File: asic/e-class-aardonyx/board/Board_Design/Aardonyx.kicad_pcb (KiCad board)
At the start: 4 copper layers, 298 parts, among them J1 USB_B_6PIN, J10 Conn_1x6_F, J11 Conn_1x6_F, J12 Conn_1x3_M, J13 Conn_1x8_F, J14 Conn_1x6_F, J15 Conn_1x10, J16 Conn_1x8_F, J17 USB_OTG, J18 Conn_1x3_M, J19 Conn_1x3_M, J2 Conn_1x8, J3 Conn_1x3_M, J4 Conn_1x4, J5 PJ-202H PWRJACK, J6 Conn_1x3_M, J7 Conn_1x4, J8 Conn_1x3_M, J9 Conn_1x8, Q1 FDN339AN, SW1 SW_SPST, SW2 FSM2JSMAATR, SW3 SW_DIP_x03, U1 FT2232H, U10 TPS7A7002DDAR, U11 ADM1085, U12 ADM1085, U13 TPS7A7002DDAR, U14 74AUP1G09GW, U15 SKT32E, U16 93LC56BT-I_OT, U2 IS42S32160F-TSOP2, U3 CDCE913PW, U4 TPS54627DDAR, U5 CAT24M01WI-GT3, U6 IS25LP256x-xM, U7 ADC108S102CIMTX, U8 LSF0108PWR, U9 LSF0108PWR, Y1 12MHz, Y2 27MHz

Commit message: Placement changes
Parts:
- moved R128 129.7 mm to (202.0, 117.0)
- moved R129 129.7 mm to (205.0, 116.9)
- moved R131 129.7 mm to (202.2, 132.6)
- moved R132 129.7 mm to (204.2, 132.6)
- moved R130 129.7 mm to (208.3, 117.0)
- moved SW3 129.7 mm to (207.5, 121.1)
- moved J11 122.3 mm to (182.1, 160.3), turned to 90 degrees
- moved J12 108.9 mm to (152.7, 150.6)
- moved U7 106.0 mm to (120.7, 146.1), turned to 90 degrees
- moved C49 103.3 mm to (117.6, 146.1)
- moved C50 103.3 mm to (130.3, 146.6)
- moved R35 103.3 mm to (117.6, 142.6)
- moved J19 80.7 mm to (147.3, 150.6), turned to 0 degrees
- moved J8 59.6 mm to (207.0, 99.6)
- moved J9 56.5 mm to (196.6, 107.7)
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
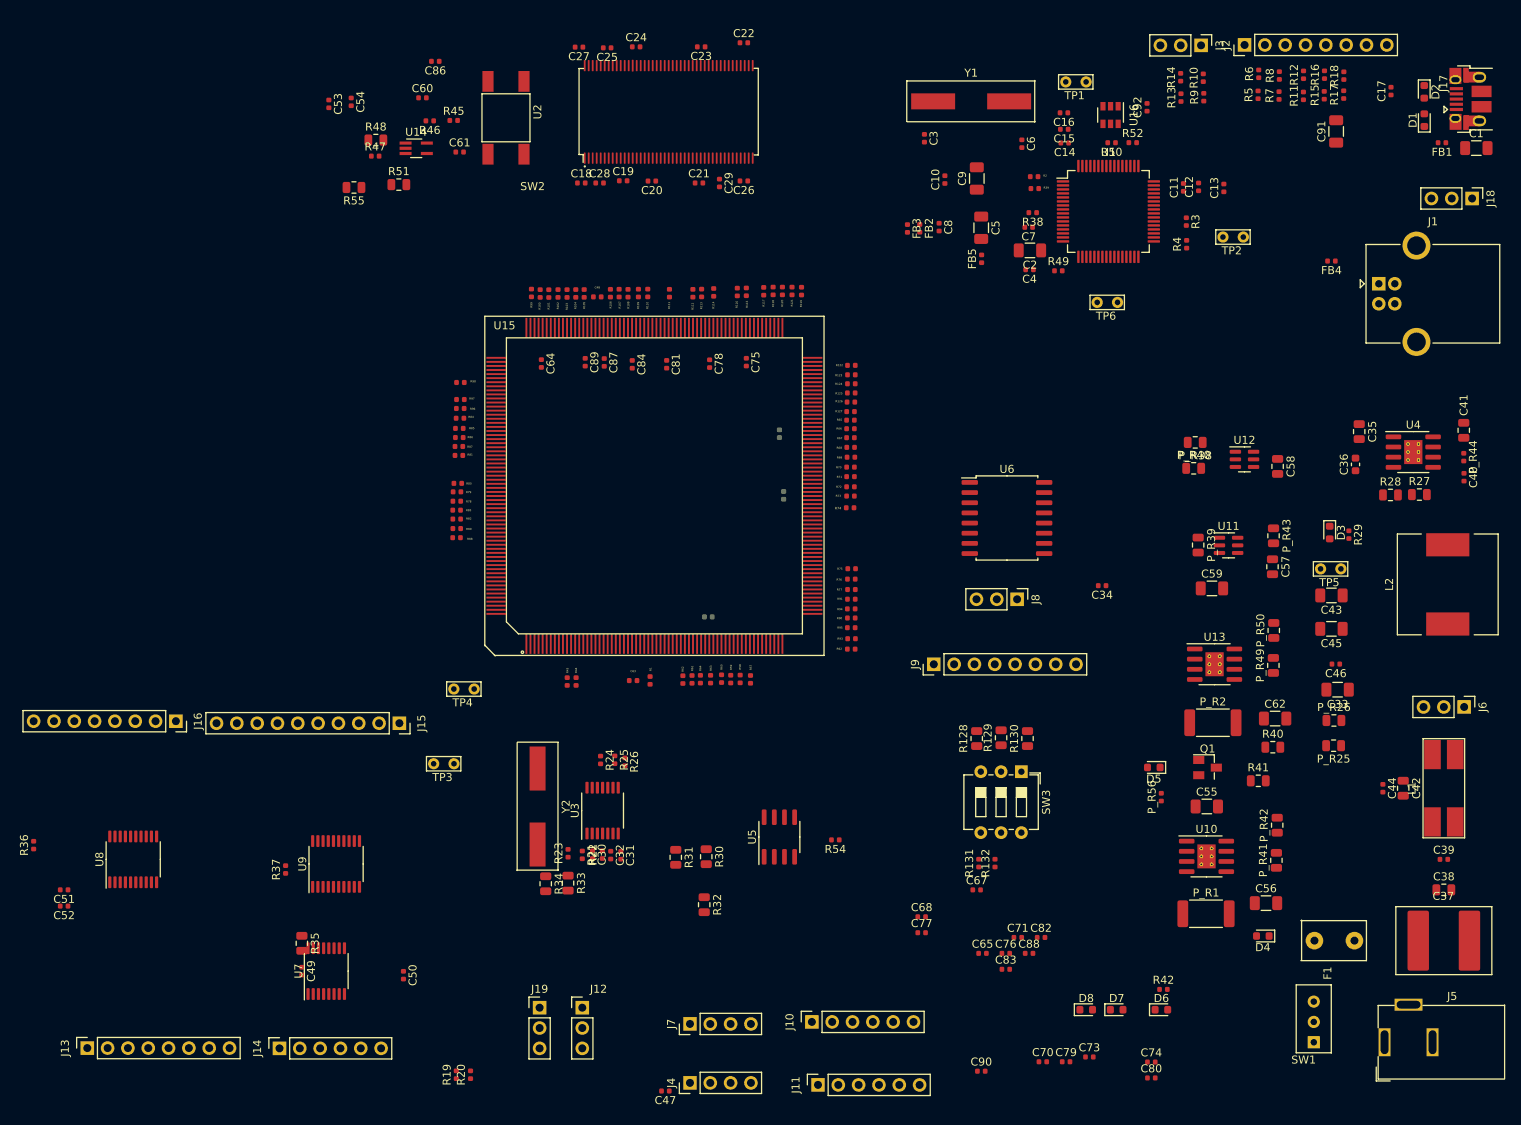
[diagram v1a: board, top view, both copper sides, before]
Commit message: updated compo placement
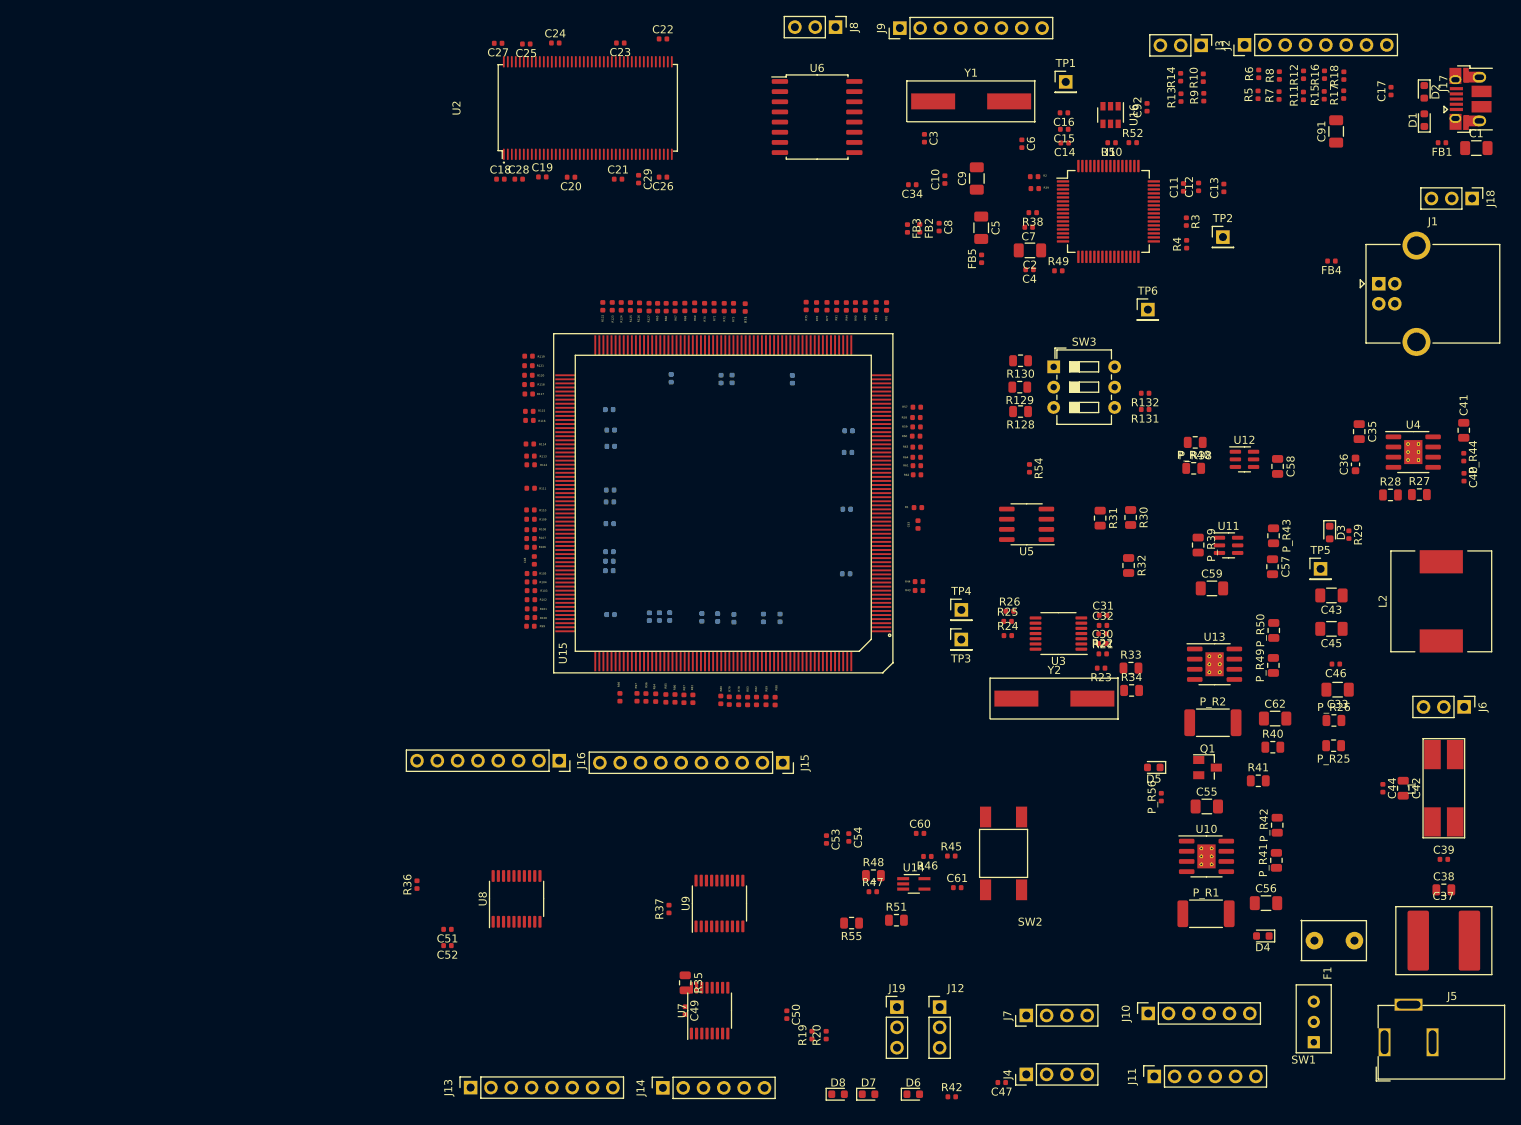
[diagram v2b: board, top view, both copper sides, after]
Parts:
- C64, C65, C67, C68, C70, C71, C73, C74, C75, C76, C77, C78, C79, C80, C81, C82, C83, C84, C86, C87, C88, C89, C90: moved to B.Cu
- TP1, TP2, TP3, TP4, TP5, TP6: footprint TestPoint:TestPoint_Bridge_Pitch2.54mm_Drill0.7mm -> Connector_PinHeader_2.54mm:PinHeader_1x01_P2.54mm_Vertical
- moved C60 111.0 mm to (194.9, 128.8)
- moved C61 111.0 mm to (199.5, 135.6)
- moved C53 111.0 mm to (183.2, 129.6)
- moved R46 111.0 mm to (195.8, 131.7)
- moved R48 111.0 mm to (189.0, 134.1)
- moved R51 111.0 mm to (191.9, 139.7)
- moved SW2 111.0 mm to (205.3, 131.3)
- moved C54 111.0 mm to (186.0, 129.3)
- moved R45 111.0 mm to (198.8, 131.7)
- moved R47 111.0 mm to (189.0, 136.1)
- moved R55 111.0 mm to (186.3, 140.0)
- moved U14 111.0 mm to (194.1, 135.1)
- moved C80 105.5 mm to (156.2, 78.4)
- moved C74 96.4 mm to (178.9, 72.1), turned to 270 degrees
- moved J9 79.6 mm to (192.3, 28.2)
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
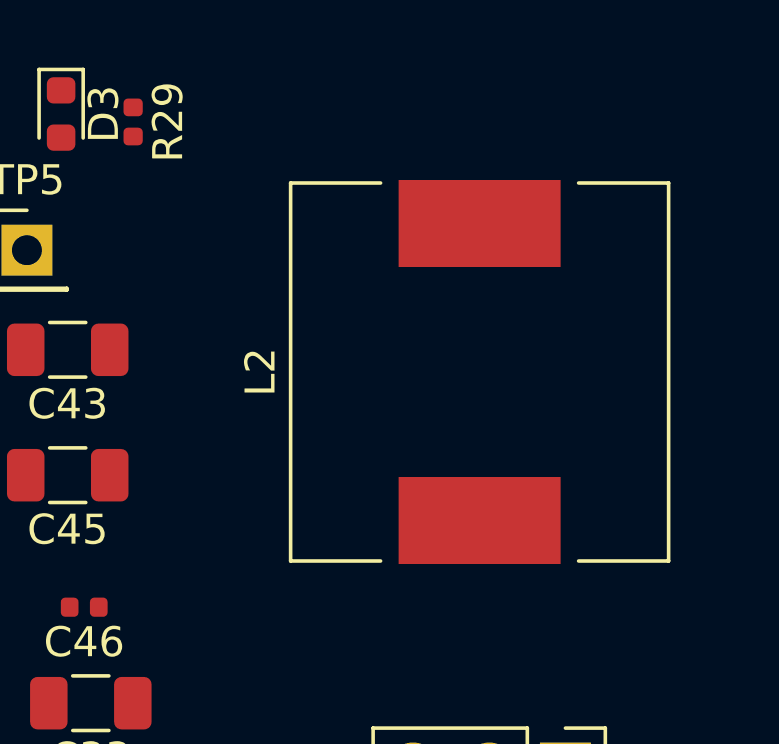
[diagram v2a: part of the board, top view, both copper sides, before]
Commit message: update footprint & bom
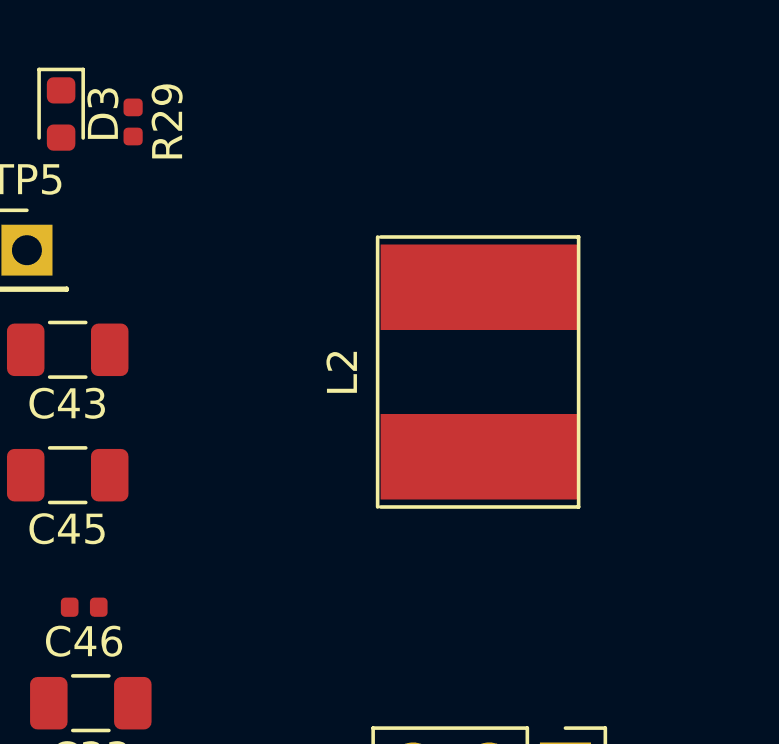
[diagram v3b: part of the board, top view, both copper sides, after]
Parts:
- L2: footprint Inductor_SMD:L_Wuerth_WE-PD-Typ-LS -> Aardonyx:Bourns_srn8040ta_L8.5_W6.6
- U7: value ADC108S102CIMTX -> ADC128S102CIMTX/NOPB
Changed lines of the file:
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@@
     (add_net ~)
   )
+  (module Aardonyx:Bourns_srn8040ta_L8.5_W6.6 (layer F.Cu)
+    (at 260.03 99.83 90)
+    (descr "Shielded Coupled Inductor, Wuerth Elektronik, WE-DD, SMD, Typ L, Typ XL, Typ XXL, https://katalog.we-online.com/pbs/datasheet/744874001.pdf")
+    (tags "Choke Coupled Double Inductor SMD Wuerth WE-DD TypL TypXL TypXXL ")
+    (attr smd)
+    (fp_text reference L2 (at -0.01016 -4.55168 90) (layer F.SilkS)
+      (effects (font (size 1 1) (thickness 0.15)))
+    )
+    (fp_text value 3.3UH (at -0.04572 4.54152 90) (layer F.Fab)
+      (effects (font (size 1 1) (thickness 0.15)))
+    )
+    (fp_line (start -4.3 -3.4) (end 4.3 -3.4) (layer F.Fab) (width 0.1))
+    (fp_line (start -4.3 3.3) (end -4.3 -3.3) (layer F.Fab) (width 0.1))
+    (fp_line (start 4.3 3.3) (end -4.3 3.3) (layer F.Fab) (width 0.1))
+    (fp_line (start 4.3 -3.3) (end 4.3 3.3) (layer F.Fab) (width 0.1))
+    (fp_line (start -4.5 3.3) (end -4.5 -3.3) (layer F.SilkS) (width 0.12))
+    (fp_line (start 4.5 3.3) (end -4.5 3.3) (layer F.SilkS) (width 0.12))
+    (fp_line (start 4.5 -3.3) (end 4.5 3.3) (layer F.SilkS) (width 0.12))
+    (fp_line (start -4.5 -3.4) (end 4.5 -3.4) (layer F.SilkS) (width 0.12))
+    (pad 2 smd rect (at 2.825 0 90) (size 2.85 6.6) (layers F.Cu F.Paste F.Mask)
+      (net 425 ~))
+    (pad 1 smd rect (at -2.825 0 90) (size 2.85 6.6) (layers F.Cu F.Paste F.Mask)
+      (net 11 "Net-(C40-Pad2)"))
+    (model ${KISYS3DMOD}/Inductor_SMD.3dshapes/L_Wuerth_WE-DD-Typ-L-Typ-XL-Typ-XXL.wrl
+      (at (xyz 0 0 0))
+      (scale (xyz 1 1 1))
+      (rotate (xyz 0 0 0))
+    )
+  )
   (module Connector_PinHeader_2.54mm:PinHeader_1x01_P2.54mm_Vertical (layer F.Cu)
     (at 223.35 63.36)
@@
     )
   )
-  (module Inductor_SMD:L_Wuerth_WE-PD-Typ-LS (layer F.Cu)
-    (at 260.03 99.83 90)
-    (descr "Shielded Power Inductor, Wuerth Elektronik, WE-PD, SMD, Typ LS, https://katalog.we-online.com/pbs/datasheet/7447715906.pdf")
-    (tags "Choke Shielded Power Inductor WE-PD TypLS Wuerth")
-    (attr smd)
-    (fp_text reference L2 (at 0 -7.3 90) (layer F.SilkS)
-      (effects (font (size 1 1) (thickness 0.15)))
-    )
-    (fp_text value 3.3UH (at 0 7.4 90) (layer F.Fab)
-      (effects (font (size 1 1) (thickness 0.15)))
-    )
-    (fp_line (start -6.2 -6.2) (end -6.2 6.2) (layer F.Fab) (width 0.1))
-    (fp_line (start 6.2 6.2) (end 6.2 -6.2) (layer F.Fab) (width 0.1))
-    (fp_line (start -6.3 -3.3) (end -6.3 -6.3) (layer F.SilkS) (width 0.12))
-    (fp_line (start -6.3 -6.3) (end 6.3 -6.3) (layer F.SilkS) (width 0.12))
-    (fp_line (start 6.3 -6.3) (end 6.3 -3.3) (layer F.SilkS) (width 0.12))
-    (fp_line (start 6.3 3.3) (end 6.3 6.3) (layer F.SilkS) (width 0.12))
-    (fp_line (start 6.3 6.3) (end -6.3 6.3) (layer F.SilkS) (width 0.12))
-    (fp_line (start -6.3 6.3) (end -6.3 3.3) (layer F.SilkS) (width 0.12))
-    (fp_line (start 6.75 6.5) (end -6.75 6.5) (layer F.CrtYd) (width 0.05))
-    (fp_line (start -6.75 6.5) (end -6.75 -6.5) (layer F.CrtYd) (width 0.05))
-    (fp_line (start -6.75 -6.5) (end 6.75 -6.5) (layer F.CrtYd) (width 0.05))
-    (fp_line (start 6.75 -6.5) (end 6.75 6.5) (layer F.CrtYd) (width 0.05))
-    (fp_line (start 4.9 3.3) (end 5 3.4) (layer F.Fab) (width 0.1))
-    (fp_line (start 5 3.4) (end 5.1 3.8) (layer F.Fab) (width 0.1))
-    (fp_line (start 5.1 3.8) (end 5 4.3) (layer F.Fab) (width 0.1))
-    (fp_line (start 5 4.3) (end 4.8 4.6) (layer F.Fab) (width 0.1))
-    (fp_line (start 4.8 4.6) (end 4.5 5) (layer F.Fab) (width 0.1))
-    (fp_line (start 4.5 5) (end 4 5.1) (layer F.Fab) (width 0.1))
-    (fp_line (start 4 5.1) (end 3.5 5) (layer F.Fab) (width 0.1))
-    (fp_line (start 3.5 5) (end 3.1 4.7) (layer F.Fab) (width 0.1))
-    (fp_line (start 3.1 4.7) (end 3 4.6) (layer F.Fab) (width 0.1))
-    (fp_line (start 3 4.6) (end 2.4 5) (layer F.Fab) (width 0.1))
-    (fp_line (start 2.4 5) (end 1.6 5.3) (layer F.Fab) (width 0.1))
-    (fp_line (start 1.6 5.3) (end 0.6 5.5) (layer F.Fab) (width 0.1))
-    (fp_line (start 0.6 5.5) (end -0.6 5.5) (layer F.Fab) (width 0.1))
-    (fp_line (start -0.6 5.5) (end -1.5 5.3) (layer F.Fab) (width 0.1))
-    (fp_line (start -1.5 5.3) (end -2.1 5.1) (layer F.Fab) (width 0.1))
-    (fp_line (start -2.1 5.1) (end -2.6 4.9) (layer F.Fab) (width 0.1))
-    (fp_line (start -2.6 4.9) (end -3 4.7) (layer F.Fab) (width 0.1))
-    (fp_line (start -3 4.7) (end -3.3 4.9) (layer F.Fab) (width 0.1))
-    (fp_line (start -3.3 4.9) (end -3.9 5.1) (layer F.Fab) (width 0.1))
-    (fp_line (start -3.9 5.1) (end -4.3 5) (layer F.Fab) (width 0.1))
-    (fp_line (start -4.3 5) (end -4.6 4.8) (layer F.Fab) (width 0.1))
-    (fp_line (start -4.6 4.8) (end -4.9 4.6) (layer F.Fab) (width 0.1))
-    (fp_line (start -4.9 4.6) (end -5.1 4.1) (layer F.Fab) (width 0.1))
-    (fp_line (start -5.1 4.1) (end -5 3.6) (layer F.Fab) (width 0.1))
-    (fp_line (start -5 3.6) (end -4.8 3.2) (layer F.Fab) (width 0.1))
-    (fp_line (start 4.9 -3.3) (end 5 -3.6) (layer F.Fab) (width 0.1))
-    (fp_line (start 5 -3.6) (end 5.1 -4) (layer F.Fab) (width 0.1))
-    (fp_line (start 5.1 -4) (end 5 -4.3) (layer F.Fab) (width 0.1))
-    (fp_line (start 5 -4.3) (end 4.8 -4.7) (layer F.Fab) (width 0.1))
-    (fp_line (start 4.8 -4.7) (end 4.5 -4.9) (layer F.Fab) (width 0.1))
-    (fp_line (start 4.5 -4.9) (end 4.2 -5.1) (layer F.Fab) (width 0.1))
-    (fp_line (start 4.2 -5.1) (end 3.9 -5.1) (layer F.Fab) (width 0.1))
-    (fp_line (start 3.9 -5.1) (end 3.6 -5) (layer F.Fab) (width 0.1))
-    (fp_line (start 3.6 -5) (end 3.3 -4.9) (layer F.Fab) (width 0.1))
-    (fp_line (start 3.3 -4.9) (end 3 -4.6) (layer F.Fab) (width 0.1))
-    (fp_line (start 3 -4.6) (end 2.6 -4.9) (layer F.Fab) (width 0.1))
-    (fp_line (start 2.6 -4.9) (end 2.2 -5.1) (layer F.Fab) (width 0.1))
-    (fp_line (start 2.2 -5.1) (end 1.7 -5.3) (layer F.Fab) (width 0.1))
-    (fp_line (start 1.7 -5.3) (end 0.9 -5.5) (layer F.Fab) (width 0.1))
-    (fp_line (start 0.9 -5.5) (end 0 -5.6) (layer F.Fab) (width 0.1))
-    (fp_line (start 0 -5.6) (end -0.8 -5.5) (layer F.Fab) (width 0.1))
-    (fp_line (start -0.8 -5.5) (end -1.7 -5.3) (layer F.Fab) (width 0.1))
-    (fp_line (start -1.7 -5.3) (end -2.6 -4.9) (layer F.Fab) (width 0.1))
-    (fp_line (start -2.6 -4.9) (end -3 -4.7) (layer F.Fab) (width 0.1))
-    (fp_line (start -3 -4.7) (end -3.3 -4.9) (layer F.Fab) (width 0.1))
-    (fp_line (start -3.3 -4.9) (end -3.7 -5.1) (layer F.Fab) (width 0.1))
-    (fp_line (start -3.7 -5.1) (end -4.2 -5) (layer F.Fab) (width 0.1))
-    (fp_line (start -4.2 -5) (end -4.6 -4.8) (layer F.Fab) (width 0.1))
-    (fp_line (start -4.6 -4.8) (end -4.9 -4.5) (layer F.Fab) (width 0.1))
-    (fp_line (start -4.9 -4.5) (end -5.1 -4) (layer F.Fab) (width 0.1))
-    (fp_line (start -5.1 -4) (end -5 -3.5) (layer F.Fab) (width 0.1))
-    (fp_line (start -5 -3.5) (end -4.8 -3.2) (layer F.Fab) (width 0.1))
-    (fp_line (start -6.2 6.2) (end 6.2 6.2) (layer F.Fab) (width 0.1))
-    (fp_line (start 6.2 -6.2) (end -6.2 -6.2) (layer F.Fab) (width 0.1))
-    (fp_circle (center 0 0) (end 0.9 0) (layer F.Adhes) (width 0.38))
-    (fp_circle (center 0 0) (end 0.55 0) (layer F.Adhes) (width 0.38))
-    (fp_circle (center 0 0) (end 0.15 0.15) (layer F.Adhes) (width 0.38))
-    (fp_circle (center -2.1 3) (end -1.8 3.25) (layer F.Fab) (width 0.1))
-    (fp_text user %R (at 0 0 90) (layer F.Fab)
-      (effects (font (size 1 1) (thickness 0.15)))
-    )
-    (pad 2 smd rect (at 4.95 0 90) (size 2.9 5.4) (layers F.Cu F.Paste F.Mask)
-      (net 425 ~))
-    (pad 1 smd rect (at -4.95 0 90) (size 2.9 5.4) (layers F.Cu F.Paste F.Mask)
-      (net 11 "Net-(C40-Pad2)"))
-    (model ${KISYS3DMOD}/Inductor_SMD.3dshapes/L_Wuerth_WE-PD-Typ-LS.wrl
-      (at (xyz 0 0 0))
-      (scale (xyz 1 1 1))
-      (rotate (xyz 0 0 0))
-    )
-  )
   (module Resistor_SMD:R_2512_6332Metric (layer F.Cu)
     (at 230.62 138.88)
@@
       (effects (font (size 1 1) (thickness 0.15)))
     )
-    (fp_text value ADC108S102CIMTX (at 0 3.45 90) (layer F.Fab)
+    (fp_text value ADC128S102CIMTX/NOPB (at 0 3.45 90) (layer F.Fab)
       (effects (font (size 1 1) (thickness 0.15)))
     )

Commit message: updated components
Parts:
- moved C34 78.7 mm to (255.5, 96.8)
- moved C27 74.0 mm to (121.0, 100.9), turned to 270 degrees
- moved C25 71.6 mm to (121.1, 97.4), turned to 270 degrees
- moved C24 69.8 mm to (121.0, 93.8), turned to 90 degrees
- moved C23 66.5 mm to (121.0, 85.7), turned to 270 degrees
- moved C22 66.1 mm to (120.5, 80.3), turned to 90 degrees
- moved P_R44 65.9 mm to (237.7, 142.7), turned to 180 degrees
- moved U2 57.0 mm to (129.1, 89.7), turned to 180 degrees
- moved C18 53.8 mm to (138.0, 100.7), turned to 90 degrees
- moved C28 51.8 mm to (138.0, 98.4), turned to 90 degrees
- moved C19 49.6 mm to (137.7, 95.4), turned to 90 degrees
- moved C20 47.0 mm to (137.7, 91.8), turned to 270 degrees
- moved C21 43.3 mm to (138.0, 85.9), turned to 90 degrees
- moved C29 42.3 mm to (138.0, 83.4), turned to 0 degrees
- moved J8 41.8 mm to (144.7, 41.5)
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
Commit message: updated component
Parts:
- added FID1: Fiducial, Fiducial:Fiducial_1.5mm_Mask3mm, F.Cu at (67.3, 96.8)
- added FID2: Fiducial, Fiducial:Fiducial_1.5mm_Mask3mm, F.Cu at (67.3, 101.3)
- added H1: MountingHole, MountingHole:MountingHole_3.5mm_Pad_Via, F.Cu at (43.7, 98.8)
- added H2: MountingHole, MountingHole:MountingHole_3.5mm_Pad_Via, F.Cu at (43.7, 107.3)
- added H3: MountingHole, MountingHole:MountingHole_3.5mm_Pad_Via, F.Cu at (52.2, 98.8)
- added H4: MountingHole, MountingHole:MountingHole_3.5mm_Pad_Via, F.Cu at (52.2, 107.3)
- added H5: MountingHole, MountingHole:MountingHole_3.5mm_Pad_Via, F.Cu at (60.8, 98.8)
- added H6: MountingHole, MountingHole:MountingHole_3.5mm_Pad_Via, F.Cu at (60.8, 107.3)
- moved R32 85.4 mm to (144.8, 56.6), turned to 90 degrees
- moved R30 81.8 mm to (144.8, 60.3)
- moved R31 81.5 mm to (144.8, 52.5), turned to 90 degrees
- moved C47 68.6 mm to (203.2, 91.4), turned to 90 degrees
- moved U6 49.8 mm to (134.4, 56.9), turned to 180 degrees
- moved R44 43.9 mm to (186.2, 140.5), turned to 270 degrees
- moved R43 42.2 mm to (190.2, 140.5), turned to 270 degrees
- moved R54 41.1 mm to (203.5, 124.0), turned to 180 degrees
- moved R34 32.0 mm to (202.2, 85.3)
- moved C48 31.7 mm to (135.7, 65.0), turned to 180 degrees
- moved R33 27.9 mm to (202.1, 87.9)
- moved R42 21.7 mm to (194.6, 140.5), turned to 270 degrees
- moved D7 17.5 mm to (189.2, 143.9)
- moved D8 17.5 mm to (185.4, 143.9)
- moved D6 17.4 mm to (193.8, 144.0)
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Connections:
- J7 pad 3: /arduino_header/I2C0_SCL -> /arduino_header/I2C0_SDA
- R33 pad 2: /arduino_header/I2C0_SCL -> /arduino_header/I2C0_SDA
- U15 pad 37: /arduino_header/I2C0_SCL -> /arduino_header/I2C0_SDA
- U5 pad 5: /arduino_header/I2C0_SCL -> /arduino_header/I2C0_SDA
